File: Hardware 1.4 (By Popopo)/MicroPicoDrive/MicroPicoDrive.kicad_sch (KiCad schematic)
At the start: 22 parts, among them IC1 SN74LVC1T45DBVR, IC2 SN74LVC1T45DBVR, IC3 TXU0304QPWRQ1, J1 Conn_02x16, J2 QL_CONN, Q1 Q_NPN_BEC, U1 LM7805_TO220, U2 Pico

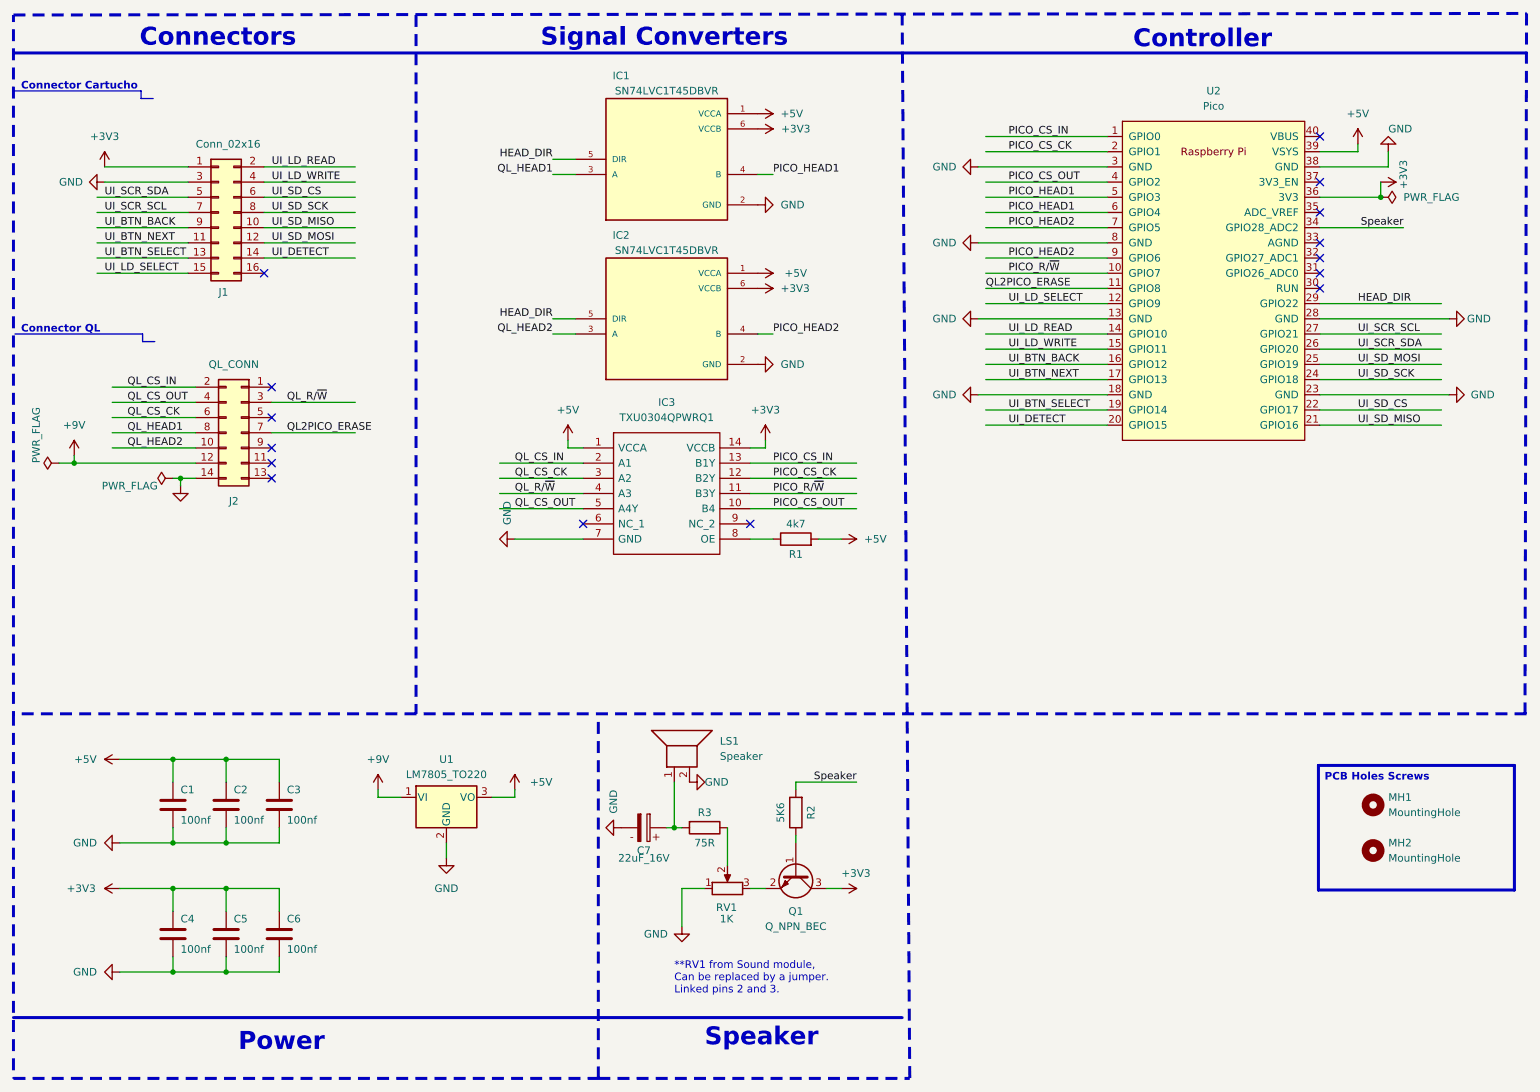
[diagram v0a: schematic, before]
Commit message: adding diode VSYS
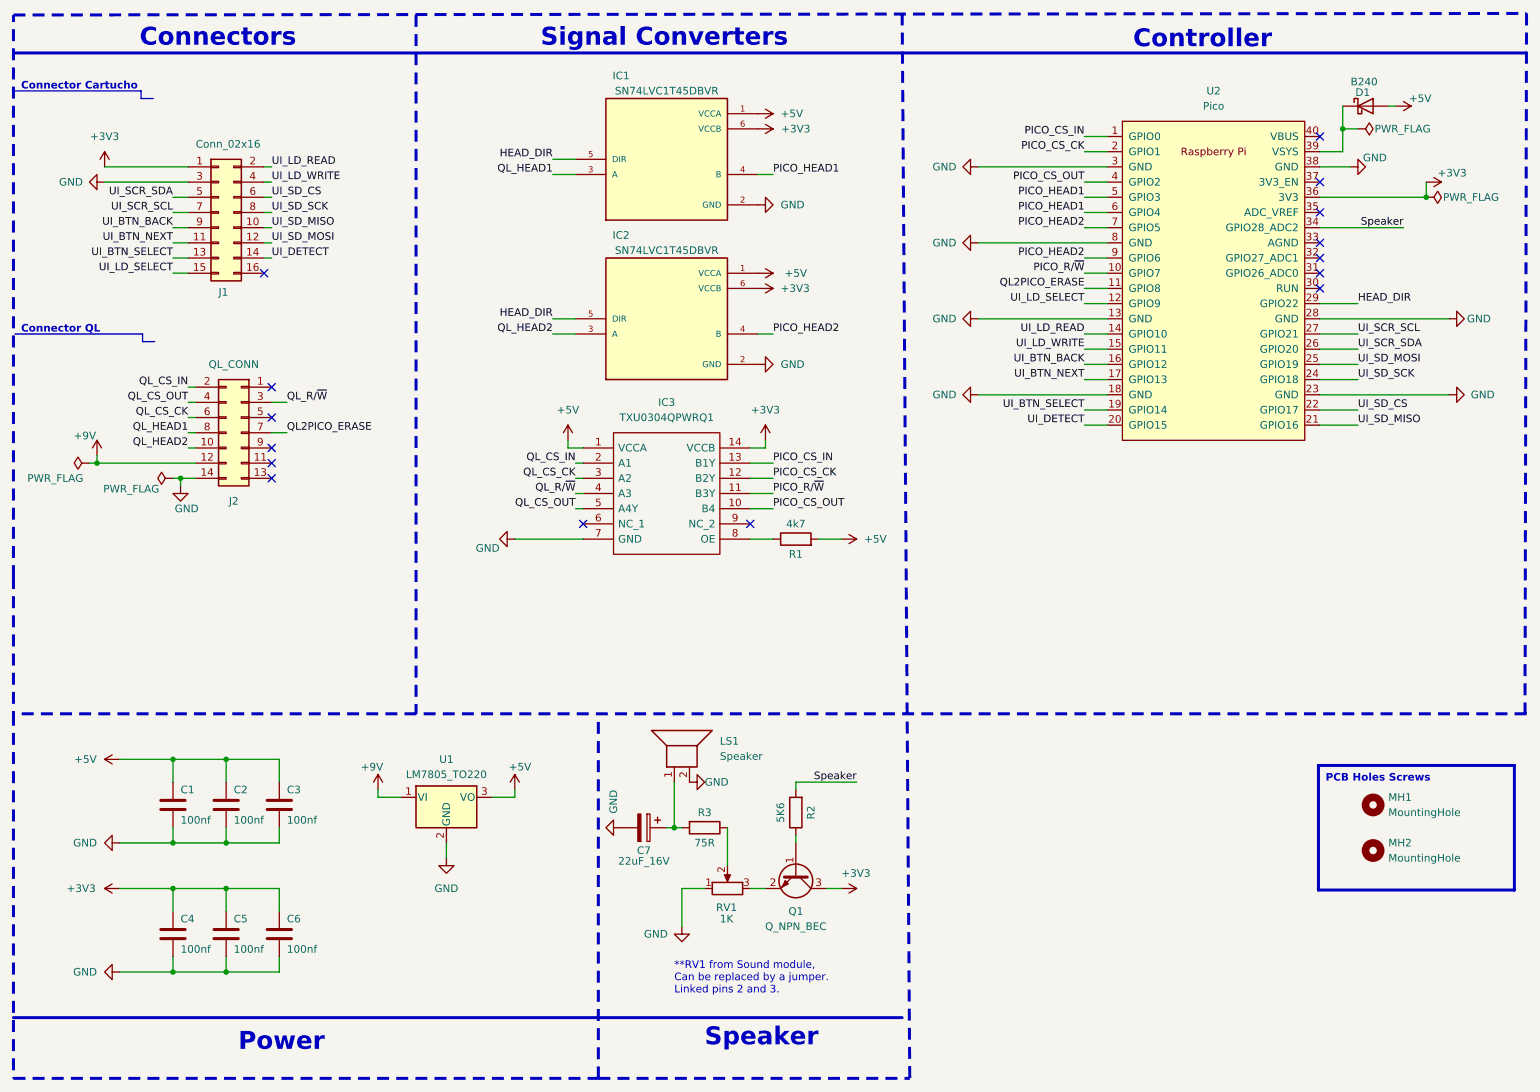
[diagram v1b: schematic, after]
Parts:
- added D1: B240, Diode_SMD:D_SMB, symbol Diode:B240
- C7: symbol PCM_SL_Capacitors:22uF_16V -> Device:C_Polarized
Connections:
- net +5V: now also D1.2 (A); no longer U2.39 (VSYS)
- new net: D1.1 (K), U2.39 (VSYS)

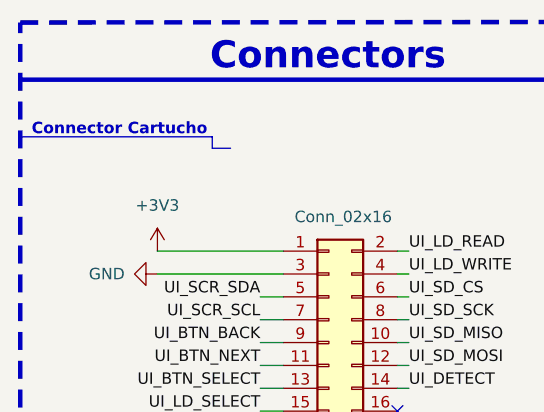
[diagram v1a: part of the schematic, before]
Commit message: Revision driver and firmware, left cartridge rev.e real test
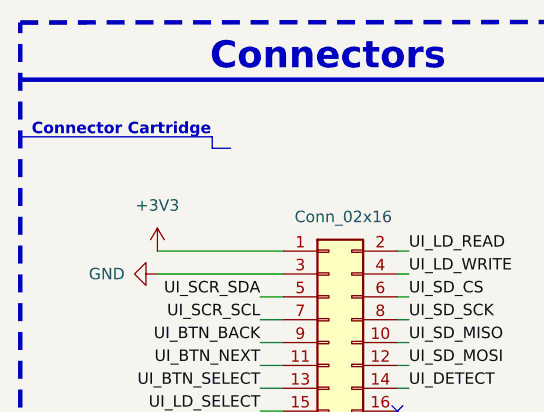
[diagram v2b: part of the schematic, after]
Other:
- note added: "Connector Cartridge"
- note removed: "Connector Cartucho"
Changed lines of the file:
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@@
 		)
 	)
-	(text "Connector Cartucho"
+	(text "Connector Cartridge"
 		(exclude_from_sim no)
 		(at 21.59 29.21 0)

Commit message: recovering hard format
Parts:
- added R4: 330R, Resistor_SMD:R_0603_1608Metric, symbol Device:R
- Q1: symbol Device:Q_NPN_BEC -> Transistor_BJT:Q_NPN_BEC
- R3: symbol PCM_Resistor_AKL:R_0805 -> Device:R
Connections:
- net GND: now also J1.16 (Pin_16)
- net UI_DETECT: now also R4.1; no longer U2.20 (GPIO15)
- new net: R4.2, U2.20 (GPIO15)
- no-connect marks 15 -> 14
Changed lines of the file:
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@@
 	)
 	(no_connect
-		(at 62.23 59.69)
-	)
-	(no_connect
 		(at 238.76 44.45)
 	)
@@
 	(wire
 		(pts
+			(xy 189.23 86.36) (xy 189.23 85.09)
+		)
+		(stroke
+			(width 0)
+			(type default)
+		)
+	)
+	(wire
+		(pts
 			(xy 49.53 86.36) (xy 50.8 86.36)
 		)
@@
 	(wire
 		(pts
-			(xy 199.39 74.93) (xy 203.2 74.93)
+			(xy 189.23 85.09) (xy 191.77 85.09)
 		)
 		(stroke
@@
 	(wire
 		(pts
-			(xy 238.76 67.31) (xy 260.35 67.31)
+			(xy 199.39 74.93) (xy 203.2 74.93)
 		)
 		(stroke
@@
 	(wire
 		(pts
-			(xy 238.76 52.07) (xy 252.73 52.07)
+			(xy 238.76 67.31) (xy 260.35 67.31)
 		)
 		(stroke
@@
 	(wire
 		(pts
-			(xy 46.99 54.61) (xy 49.53 54.61)
+			(xy 238.76 52.07) (xy 252.73 52.07)
 		)
 		(stroke
@@
 	(wire
 		(pts
-			(xy 38.1 176.53) (xy 46.99 176.53)
+			(xy 46.99 54.61) (xy 49.53 54.61)
 		)
 		(stroke
@@
 	(wire
 		(pts
-			(xy 238.76 85.09) (xy 245.11 85.09)
+			(xy 38.1 176.53) (xy 46.99 176.53)
 		)
 		(stroke
@@
 	(wire
 		(pts
-			(xy 115.57 88.9) (xy 113.03 88.9)
+			(xy 238.76 85.09) (xy 245.11 85.09)
 		)
 		(stroke
@@
 	(wire
 		(pts
-			(xy 130.81 152.4) (xy 129.54 152.4)
+			(xy 115.57 88.9) (xy 113.03 88.9)
 		)
 		(stroke
@@
 	(wire
 		(pts
-			(xy 199.39 85.09) (xy 203.2 85.09)
+			(xy 130.81 152.4) (xy 129.54 152.4)
 		)
 		(stroke
@@
 	(wire
 		(pts
+			(xy 62.23 59.69) (xy 63.5 59.69)
+		)
+		(stroke
+			(width 0)
+			(type default)
+		)
+	)
+	(wire
+		(pts
 			(xy 55.88 162.56) (xy 64.77 162.56)
 		)
@@
 	(wire
 		(pts
+			(xy 199.39 85.09) (xy 203.2 85.09)
+		)
+		(stroke
+			(width 0)
+			(type default)
+		)
+	)
+	(wire
+		(pts
 			(xy 238.76 64.77) (xy 245.11 64.77)
 		)
@@
 		)
 	)
+	(wire
+		(pts
+			(xy 187.96 86.36) (xy 189.23 86.36)
+		)
+		(stroke
+			(width 0)
+			(type default)
+		)
+	)
 	(polyline
 		(pts
@@
 	)
 	(label "UI_DETECT"
-		(at 199.39 85.09 180)
+		(at 187.96 86.36 180)
 		(effects
 			(font
@@
 	)
 	(symbol
-		(lib_id "PCM_Resistor_AKL:R_0805")
+		(lib_id "Device:R")
 		(at 135.89 152.4 270)
 		(unit 1)
@@
 		)
 		(property "Value" "75R"
-			(at 135.89 154.94 90)
+			(at 135.89 152.4 90)
 			(effects
 				(font
@@
 		)
 		(property "Footprint" "Resistor_THT:R_Axial_DIN0207_L6.3mm_D2.5mm_P10.16mm_Horizontal"
-			(at 124.46 152.4 0)
+			(at 135.89 150.622 90)
 			(effects
 				(font
@@
 			)
 		)
-		(property "Description" ""
+		(property "Description" "Resistor"
 			(at 135.89 152.4 0)
 			(effects
@@
 		)
 		(property "Value" "4k7"
-			(at 151.13 101.6 90)
+			(at 151.13 104.14 90)
 			(effects
 				(font
@@
 	)
 	(symbol
+		(lib_id "Device:R")
+		(at 195.58 85.09 90)
+		(unit 1)
+		(exclude_from_sim no)
+		(in_bom yes)
+		(on_board yes)
+		(dnp no)
+		(property "Reference" "R4"
+			(at 195.58 87.63 90)
+			(effects
+				(font
+					(size 1.27 1.27)
+				)
+			)
+		)
+		(property "Value" "330R"
+			(at 195.58 85.09 90)
+			(effects
+				(font
+					(size 1.27 1.27)
+				)
+			)
+		)
+		(property "Footprint" "Resistor_SMD:R_0603_1608Metric"
+			(at 195.58 86.868 90)
+			(effects
+				(font
+					(size 1.27 1.27)
+				)
+				(hide yes)
+			)
+		)
+		(property "Datasheet" "~"
+			(at 195.58 85.09 0)
+			(effects
+				(font
+					(size 1.27 1.27)
+				)
+				(hide yes)
+			)
+		)
+		(property "Description" ""
+			(at 195.58 85.09 0)
+			(effects
+				(font
+					(size 1.27 1.27)
+				)
+				(hide yes)
+			)
+		)
+		(pin "1"
+		)
+		(pin "2"
+		)
+		(instances
+			(project "MicroPicoDrive"
+				(path "/f4d392c7-1fac-442d-8754-ed592ab7a8b5"
+					(reference "R4")
+					(unit 1)
+				)
+			)
+		)
+	)
+	(symbol
 		(lib_id "MicroPicoDrive:TXU0304QPWRQ1")
 		(at 115.57 88.9 0)
@@
 	(symbol
 		(lib_id "power:GND")
+		(at 63.5 59.69 90)
+		(mirror x)
+		(unit 1)
+		(exclude_from_sim no)
+		(in_bom yes)
+		(on_board yes)
+		(dnp no)
+		(property "Reference" "#PWR035"
+			(at 69.85 59.69 0)
+			(effects
+				(font
+					(size 1.27 1.27)
+				)
+				(hide yes)
+			)
+		)
+		(property "Value" "GND"
+			(at 71.12 59.69 90)
+			(effects
+				(font
+					(size 1.27 1.27)
+				)
+				(justify left)
+			)
+		)
+		(property "Footprint" ""
+			(at 63.5 59.69 0)
+			(effects
+				(font
+					(size 1.27 1.27)
+				)
+				(hide yes)
+			)
+		)
+		(property "Datasheet" ""
+			(at 63.5 59.69 0)
+			(effects
+				(font
+					(size 1.27 1.27)
+				)
+				(hide yes)
+			)
+		)
+		(property "Description" "Power symbol creates a global label with name \"GND\" , ground"
+			(at 63.5 59.69 0)
+			(effects
+				(font
+					(size 1.27 1.27)
+				)
+				(hide yes)
+			)
+		)
+		(pin "1"
+		)
+		(instances
+			(project "MicroPicoDrive"
+				(path "/f4d392c7-1fac-442d-8754-ed592ab7a8b5"
+					(reference "#PWR035")
+					(unit 1)
+				)
+			)
+		)
+	)
+	(symbol
+		(lib_id "power:GND")
 		(at 181.61 54.61 270)
 		(mirror x)
@@
 		)
 		(property "Value" "5K6"
-			(at 148.59 149.86 90)
+			(at 151.13 149.86 90)
 			(effects
 				(font
@@
 		)
 		(property "Value" "1K"
-			(at 138.43 167.64 90)
+			(at 138.43 162.56 90)
 			(effects
 				(font
@@
 	)
 	(symbol
-		(lib_id "Device:Q_NPN_BEC")
+		(lib_id "Transistor_BJT:Q_NPN_BEC")
 		(at 151.13 160.02 270)
 		(unit 1)
@@
 			(at 151.13 160.02 0)
 			(effects
+				(font
+					(size 1.27 1.27)
+				)
+				(hide yes)
+			)
+		)
+		(property "Sim.Device" "NPN"
+			(at 151.13 160.02 0)
+			(effects
+				(font
+					(size 1.27 1.27)
+				)
+				(hide yes)
+			)
+		)
+		(property "Sim.Pins" "1=B 2=E 3=C"
+			(at 151.13 160.02 0)
+			(effects

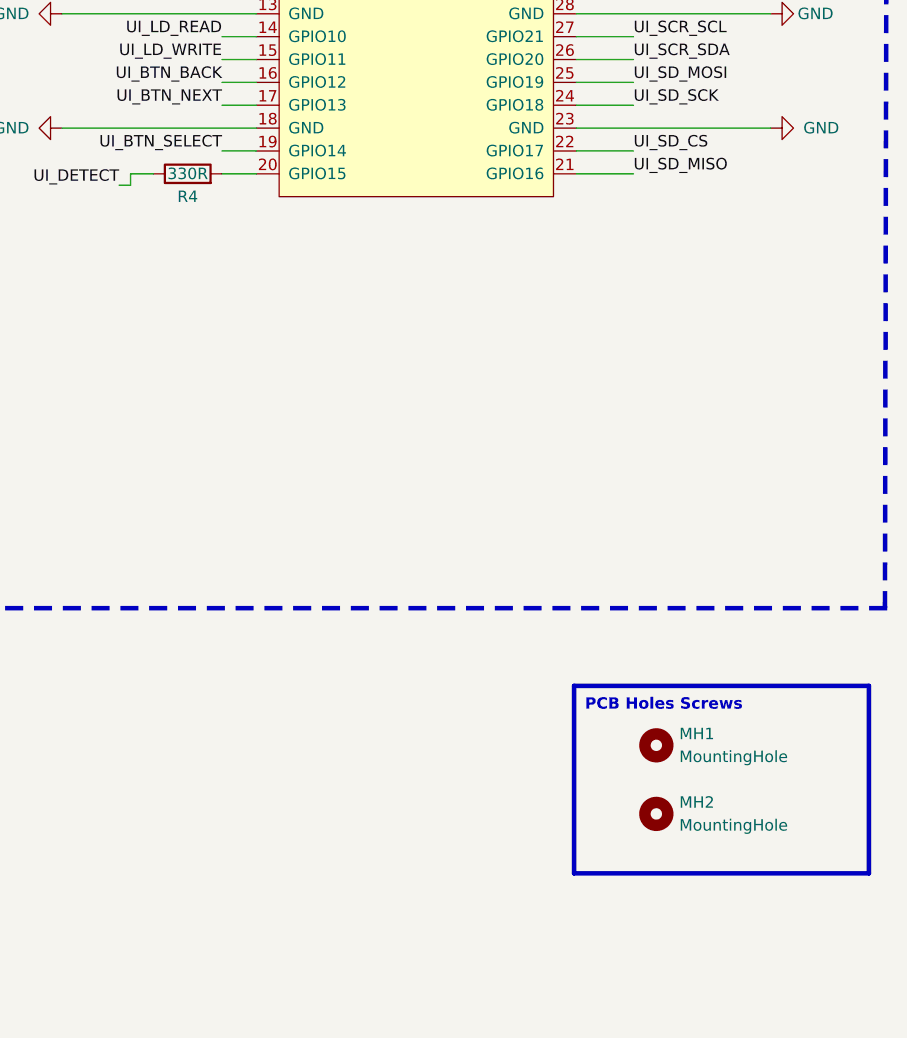
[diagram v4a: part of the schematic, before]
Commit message: changing DRC and PCB references 2
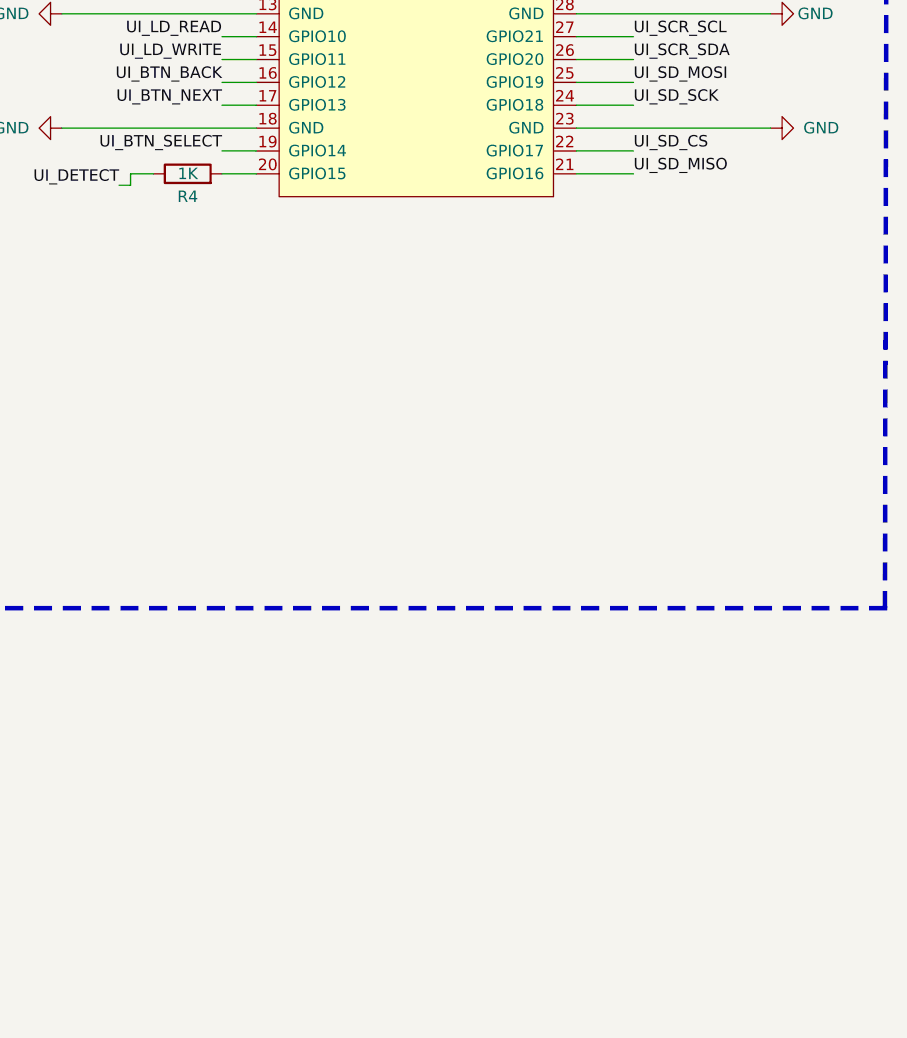
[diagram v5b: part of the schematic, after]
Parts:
- removed MH1, MH2: MountingHole, MicroPicoDrive_Driver:MountingHole_3.5mm_safe_screw_area, symbol Mechanical:MountingHole
- R4: value 330R -> 1K
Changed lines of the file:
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@@
 		)
 	)
-	(text_box "PCB Holes Screws"
-		(exclude_from_sim no)
-		(at 238.506 141.986 0)
-		(size 32.766 20.828)
-		(margins 1.2025 1.2025 1.2025 1.2025)
-		(stroke
-			(width 0.5)
-			(type default)
-		)
-		(fill
-			(type none)
-		)
-		(effects
-			(font
-				(size 1.27 1.27)
-				(bold yes)
-			)
-			(justify left top)
-		)
-	)
 	(junction
 		(at 46.99 176.53)
@@
 			)
 		)
-		(property "Value" "330R"
+		(property "Value" "1K"
 			(at 195.58 85.09 90)
 			(effects
@@
 	)
 	(symbol
-		(lib_id "Mechanical:MountingHole")
-		(at 247.65 148.59 0)
-		(unit 1)
-		(exclude_from_sim no)
-		(in_bom yes)
-		(on_board yes)
-		(dnp no)
-		(fields_autoplaced yes)
-		(property "Reference" "MH1"
-			(at 250.19 147.32 0)
-			(effects
-				(font
-					(size 1.27 1.27)
-				)
-				(justify left)
-			)
-		)
-		(property "Value" "MountingHole"
-			(at 250.19 149.86 0)
-			(effects
-				(font
-					(size 1.27 1.27)
-				)
-				(justify left)
-			)
-		)
-		(property "Footprint" "MicroPicoDrive_Driver:MountingHole_3.5mm_safe_screw_area"
-			(at 247.65 148.59 0)
-			(effects
-				(font
-					(size 1.27 1.27)
-				)
-				(hide yes)
-			)
-		)
-		(property "Datasheet" "~"
-			(at 247.65 148.59 0)
-			(effects
-				(font
-					(size 1.27 1.27)
-				)
-				(hide yes)
-			)
-		)
-		(property "Description" ""
-			(at 247.65 148.59 0)
-			(effects
-				(font
-					(size 1.27 1.27)
-				)
-				(hide yes)
-			)
-		)
-		(instances
-			(project "MicroPicoDrive"
-				(path "/f4d392c7-1fac-442d-8754-ed592ab7a8b5"
-					(reference "MH1")
-					(unit 1)
-				)
-			)
-		)
-	)
-	(symbol
 		(lib_id "power:PWR_FLAG")
 		(at 256.54 46.99 270)
@@
 					(unit 1)
 				)
-			)
-		)
-	)
-	(symbol
-		(lib_id "Mechanical:MountingHole")
-		(at 247.65 156.21 0)
-		(unit 1)
-		(exclude_from_sim no)
-		(in_bom yes)
-		(on_board yes)
-		(dnp no)
-		(fields_autoplaced yes)
-		(property "Reference" "MH2"
-			(at 250.19 154.94 0)
-			(effects
-				(font
-					(size 1.27 1.27)
-				)
-				(justify left)
-			)
-		)
-		(property "Value" "MountingHole"
-			(at 250.19 157.48 0)
-			(effects
-				(font
-					(size 1.27 1.27)
-				)
-				(justify left)
-			)
-		)
-		(property "Footprint" "MicroPicoDrive_Driver:MountingHole_3.5mm_safe_screw_area"
-			(at 247.65 156.21 0)
-			(effects
-				(font
-					(size 1.27 1.27)
-				)
-				(hide yes)
-			)
-		)
-		(property "Datasheet" "~"
-			(at 247.65 156.21 0)
-			(effects
-				(font
-					(size 1.27 1.27)
-				)
-				(hide yes)
-			)
-		)
-		(property "Description" ""
-			(at 247.65 156.21 0)
-			(effects
-				(font
-					(size 1.27 1.27)
-				)
-				(hide yes)
-			)
-		)
-		(instances
-			(project "MicroPicoDrive"
-				(path "/f4d392c7-1fac-442d-8754-ed592ab7a8b5"
-					(reference "MH2")
-					(unit 1)
-				)
